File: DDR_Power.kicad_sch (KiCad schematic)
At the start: 10 parts, among them U17001 NCP114AMX250TCG

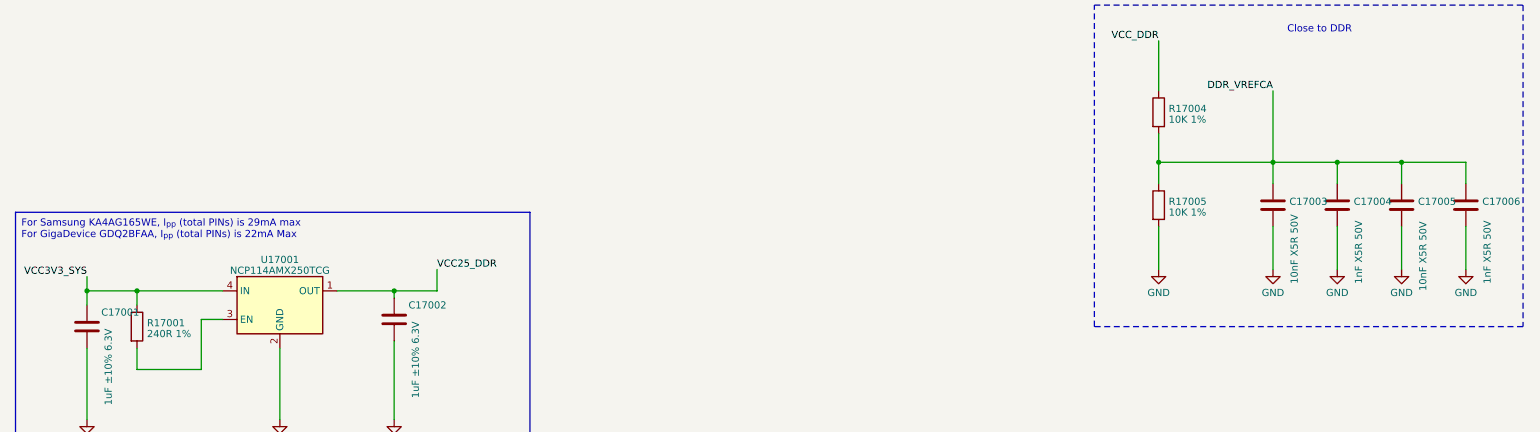
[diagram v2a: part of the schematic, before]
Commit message: move DDR power decoupling capacitors into DDR4 Sheet
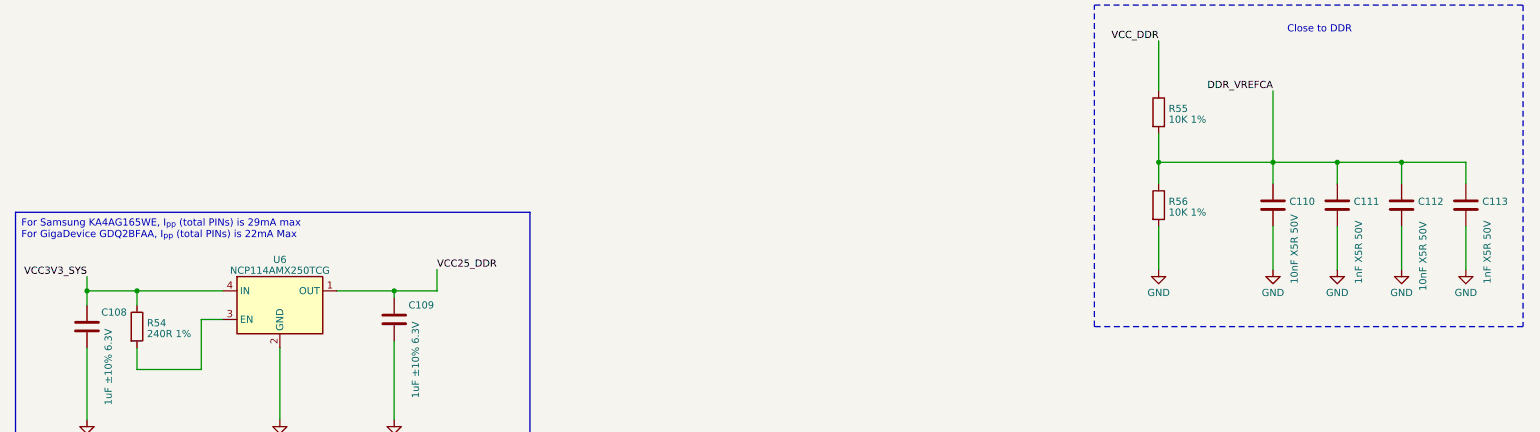
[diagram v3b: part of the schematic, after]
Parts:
- renumbered C17001 to C108, C17002 to C109, C17003 to C110, C17004 to C111, C17005 to C112, C17006 to C113, R17001 to R54, R17004 to R55, R17005 to R56, U17001 to U6
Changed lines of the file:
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@@
   (symbol (lib_id "Device:R") (at 38.1 165.1 0) (unit 1)
     (in_bom yes) (on_board yes) (dnp no) (fields_autoplaced)
-    (property "Reference" "R17001" (at 39.878 164.4563 0)
+    (property "Reference" "R54" (at 39.878 164.4563 0)
       (effects (font (size 1.27 1.27)) (justify left))
     )
@@
       (project "leaf"
         (path "/e3b58043-16a3-43c8-9fad-9c9784eebfa4/9453ad46-b3ff-4d4e-8aa6-7cc75aa0f522/f6658df5-193a-49b6-ab60-4ac3c0bbbc45"
-          (reference "R17001") (unit 1)
+          (reference "R54") (unit 1)
         )
       )
@@
   (symbol (lib_id "Device:R") (at 219.71 143.51 0) (unit 1)
     (in_bom yes) (on_board yes) (dnp no) (fields_autoplaced)
-    (property "Reference" "R17005" (at 221.488 142.8663 0)
+    (property "Reference" "R56" (at 221.488 142.8663 0)
       (effects (font (size 1.27 1.27)) (justify left))
     )
@@
       (project "leaf"
         (path "/e3b58043-16a3-43c8-9fad-9c9784eebfa4/9453ad46-b3ff-4d4e-8aa6-7cc75aa0f522/f6658df5-193a-49b6-ab60-4ac3c0bbbc45"
-          (reference "R17005") (unit 1)
+          (reference "R56") (unit 1)
         )
       )
@@
   (symbol (lib_id "Device:R") (at 219.71 127 0) (unit 1)
     (in_bom yes) (on_board yes) (dnp no) (fields_autoplaced)
-    (property "Reference" "R17004" (at 221.488 126.3563 0)
+    (property "Reference" "R55" (at 221.488 126.3563 0)
       (effects (font (size 1.27 1.27)) (justify left))
     )
@@
       (project "leaf"
         (path "/e3b58043-16a3-43c8-9fad-9c9784eebfa4/9453ad46-b3ff-4d4e-8aa6-7cc75aa0f522/f6658df5-193a-49b6-ab60-4ac3c0bbbc45"
-          (reference "R17004") (unit 1)
+          (reference "R55") (unit 1)
         )
       )
@@
   (symbol (lib_id "Leaf_Regulator_Linear:NCP114") (at 63.5 161.29 0) (unit 1)
     (in_bom yes) (on_board yes) (dnp no) (fields_autoplaced)
-    (property "Reference" "U17001" (at 63.5 153.2001 0)
+    (property "Reference" "U6" (at 63.5 153.2001 0)
       (effects (font (size 1.27 1.27)))
     )
@@
       (project "leaf"
         (path "/e3b58043-16a3-43c8-9fad-9c9784eebfa4/9453ad46-b3ff-4d4e-8aa6-7cc75aa0f522/f6658df5-193a-49b6-ab60-4ac3c0bbbc45"
-          (reference "U17001") (unit 1)
+          (reference "U6") (unit 1)
         )
       )
@@
   (symbol (lib_id "Device:C") (at 29.21 165.1 0) (unit 1)
     (in_bom yes) (on_board yes) (dnp no)
-    (property "Reference" "C17001" (at 31.75 162.56 0)
+    (property "Reference" "C108" (at 31.75 162.56 0)
       (effects (font (size 1.27 1.27)) (justify left))
     )
@@
       (project "leaf"
         (path "/e3b58043-16a3-43c8-9fad-9c9784eebfa4/9453ad46-b3ff-4d4e-8aa6-7cc75aa0f522/f6658df5-193a-49b6-ab60-4ac3c0bbbc45"
-          (reference "C17001") (unit 1)
+          (reference "C108") (unit 1)
         )
       )
@@
   (symbol (lib_id "Device:C") (at 262.89 143.51 0) (unit 1)
     (in_bom yes) (on_board yes) (dnp no)
-    (property "Reference" "C17005" (at 265.811 142.8663 0)
+    (property "Reference" "C112" (at 265.811 142.8663 0)
       (effects (font (size 1.27 1.27)) (justify left))
     )
@@
       (project "leaf"
         (path "/e3b58043-16a3-43c8-9fad-9c9784eebfa4/9453ad46-b3ff-4d4e-8aa6-7cc75aa0f522/f6658df5-193a-49b6-ab60-4ac3c0bbbc45"
-          (reference "C17005") (unit 1)
+          (reference "C112") (unit 1)
         )
       )
@@
   (symbol (lib_id "power:GND") (at 262.89 154.94 0) (unit 1)
     (in_bom yes) (on_board yes) (dnp no) (fields_autoplaced)
-    (property "Reference" "#PWR017011" (at 262.89 161.29 0)
+    (property "Reference" "#PWR0114" (at 262.89 161.29 0)
       (effects (font (size 1.27 1.27)) hide)
     )
@@
       (project "leaf"
         (path "/e3b58043-16a3-43c8-9fad-9c9784eebfa4/9453ad46-b3ff-4d4e-8aa6-7cc75aa0f522/f6658df5-193a-49b6-ab60-4ac3c0bbbc45"
-          (reference "#PWR017011") (unit 1)
+          (reference "#PWR0114") (unit 1)
         )
       )
@@
   (symbol (lib_id "power:GND") (at 29.21 181.61 0) (unit 1)
     (in_bom yes) (on_board yes) (dnp no) (fields_autoplaced)
-    (property "Reference" "#PWR017001" (at 29.21 187.96 0)
+    (property "Reference" "#PWR0108" (at 29.21 187.96 0)
       (effects (font (size 1.27 1.27)) hide)
     )
@@
       (project "leaf"
         (path "/e3b58043-16a3-43c8-9fad-9c9784eebfa4/9453ad46-b3ff-4d4e-8aa6-7cc75aa0f522/f6658df5-193a-49b6-ab60-4ac3c0bbbc45"
-          (reference "#PWR017001") (unit 1)
+          (reference "#PWR0108") (unit 1)
         )
       )
@@
   (symbol (lib_id "power:GND") (at 83.82 181.61 0) (unit 1)
     (in_bom yes) (on_board yes) (dnp no) (fields_autoplaced)
-    (property "Reference" "#PWR017003" (at 83.82 187.96 0)
+    (property "Reference" "#PWR0110" (at 83.82 187.96 0)
       (effects (font (size 1.27 1.27)) hide)
     )
@@
       (project "leaf"
         (path "/e3b58043-16a3-43c8-9fad-9c9784eebfa4/9453ad46-b3ff-4d4e-8aa6-7cc75aa0f522/f6658df5-193a-49b6-ab60-4ac3c0bbbc45"
-          (reference "#PWR017003") (unit 1)
+          (reference "#PWR0110") (unit 1)
         )
       )
@@
   (symbol (lib_id "Device:C") (at 240.03 143.51 0) (unit 1)
     (in_bom yes) (on_board yes) (dnp no)
-    (property "Reference" "C17003" (at 242.951 142.8663 0)
+    (property "Reference" "C110" (at 242.951 142.8663 0)
       (effects (font (size 1.27 1.27)) (justify left))
     )
@@
       (project "leaf"
         (path "/e3b58043-16a3-43c8-9fad-9c9784eebfa4/9453ad46-b3ff-4d4e-8aa6-7cc75aa0f522/f6658df5-193a-49b6-ab60-4ac3c0bbbc45"
-          (reference "C17003") (unit 1)
+          (reference "C110") (unit 1)
         )
       )
@@
   (symbol (lib_id "power:GND") (at 63.5 181.61 0) (unit 1)
     (in_bom yes) (on_board yes) (dnp no) (fields_autoplaced)
-    (property "Reference" "#PWR017002" (at 63.5 187.96 0)
+    (property "Reference" "#PWR0109" (at 63.5 187.96 0)
       (effects (font (size 1.27 1.27)) hide)
     )
@@
       (project "leaf"
         (path "/e3b58043-16a3-43c8-9fad-9c9784eebfa4/9453ad46-b3ff-4d4e-8aa6-7cc75aa0f522/f6658df5-193a-49b6-ab60-4ac3c0bbbc45"
-          (reference "#PWR017002") (unit 1)
+          (reference "#PWR0109") (unit 1)
         )
       )
@@
   (symbol (lib_id "power:GND") (at 219.71 154.94 0) (unit 1)
     (in_bom yes) (on_board yes) (dnp no) (fields_autoplaced)
-    (property "Reference" "#PWR017008" (at 219.71 161.29 0)
+    (property "Reference" "#PWR0111" (at 219.71 161.29 0)
       (effects (font (size 1.27 1.27)) hide)
     )
@@
       (project "leaf"
         (path "/e3b58043-16a3-43c8-9fad-9c9784eebfa4/9453ad46-b3ff-4d4e-8aa6-7cc75aa0f522/f6658df5-193a-49b6-ab60-4ac3c0bbbc45"
-          (reference "#PWR017008") (unit 1)
+          (reference "#PWR0111") (unit 1)
         )
       )
@@
   (symbol (lib_id "power:GND") (at 240.03 154.94 0) (unit 1)
     (in_bom yes) (on_board yes) (dnp no) (fields_autoplaced)
-    (property "Reference" "#PWR017009" (at 240.03 161.29 0)
+    (property "Reference" "#PWR0112" (at 240.03 161.29 0)
       (effects (font (size 1.27 1.27)) hide)
     )
@@
       (project "leaf"
         (path "/e3b58043-16a3-43c8-9fad-9c9784eebfa4/9453ad46-b3ff-4d4e-8aa6-7cc75aa0f522/f6658df5-193a-49b6-ab60-4ac3c0bbbc45"
-          (reference "#PWR017009") (unit 1)
+          (reference "#PWR0112") (unit 1)
         )
       )
@@
   (symbol (lib_id "power:GND") (at 274.32 154.94 0) (unit 1)
     (in_bom yes) (on_board yes) (dnp no) (fields_autoplaced)
-    (property "Reference" "#PWR017012" (at 274.32 161.29 0)
+    (property "Reference" "#PWR0115" (at 274.32 161.29 0)
       (effects (font (size 1.27 1.27)) hide)
     )
@@
       (project "leaf"
         (path "/e3b58043-16a3-43c8-9fad-9c9784eebfa4/9453ad46-b3ff-4d4e-8aa6-7cc75aa0f522/f6658df5-193a-49b6-ab60-4ac3c0bbbc45"
-          (reference "#PWR017012") (unit 1)
+          (reference "#PWR0115") (unit 1)
         )
       )
@@
   (symbol (lib_id "Device:C") (at 274.32 143.51 0) (unit 1)
     (in_bom yes) (on_board yes) (dnp no)
-    (property "Reference" "C17006" (at 277.241 142.8663 0)
+    (property "Reference" "C113" (at 277.241 142.8663 0)
       (effects (font (size 1.27 1.27)) (justify left))
     )
@@
       (project "leaf"
         (path "/e3b58043-16a3-43c8-9fad-9c9784eebfa4/9453ad46-b3ff-4d4e-8aa6-7cc75aa0f522/f6658df5-193a-49b6-ab60-4ac3c0bbbc45"
-          (reference "C17006") (unit 1)
+          (reference "C113") (unit 1)
         )
       )
@@
   (symbol (lib_id "Device:C") (at 251.46 143.51 0) (unit 1)
     (in_bom yes) (on_board yes) (dnp no)
-    (property "Reference" "C17004" (at 254.381 142.8663 0)
+    (property "Reference" "C111" (at 254.381 142.8663 0)
       (effects (font (size 1.27 1.27)) (justify left))
     )
@@
       (project "leaf"
         (path "/e3b58043-16a3-43c8-9fad-9c9784eebfa4/9453ad46-b3ff-4d4e-8aa6-7cc75aa0f522/f6658df5-193a-49b6-ab60-4ac3c0bbbc45"
-          (reference "C17004") (unit 1)
+          (reference "C111") (unit 1)
         )
       )
@@
   (symbol (lib_id "Device:C") (at 83.82 163.83 0) (unit 1)
     (in_bom yes) (on_board yes) (dnp no)
-    (property "Reference" "C17002" (at 86.36 161.29 0)
+    (property "Reference" "C109" (at 86.36 161.29 0)
       (effects (font (size 1.27 1.27)) (justify left))
     )
@@
       (project "leaf"
         (path "/e3b58043-16a3-43c8-9fad-9c9784eebfa4/9453ad46-b3ff-4d4e-8aa6-7cc75aa0f522/f6658df5-193a-49b6-ab60-4ac3c0bbbc45"
-          (reference "C17002") (unit 1)
+          (reference "C109") (unit 1)
         )
       )
@@
   (symbol (lib_id "power:GND") (at 251.46 154.94 0) (unit 1)
     (in_bom yes) (on_board yes) (dnp no) (fields_autoplaced)
-    (property "Reference" "#PWR017010" (at 251.46 161.29 0)
+    (property "Reference" "#PWR0113" (at 251.46 161.29 0)
       (effects (font (size 1.27 1.27)) hide)
     )
@@
       (project "leaf"
         (path "/e3b58043-16a3-43c8-9fad-9c9784eebfa4/9453ad46-b3ff-4d4e-8aa6-7cc75aa0f522/f6658df5-193a-49b6-ab60-4ac3c0bbbc45"
-          (reference "#PWR017010") (unit 1)
-        )
-      )
+          (reference "#PWR0113") (unit 1)
+        )
+      )

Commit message: changed Power Label and copy DDR4 Sheets
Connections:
- net VCC25_DDR renamed VCC2V5_DDR
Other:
- moved on the sheet: C108, C109, C110, C111, C112, C113, R54, R55, R56, U6
